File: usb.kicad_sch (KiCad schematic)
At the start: 13 parts

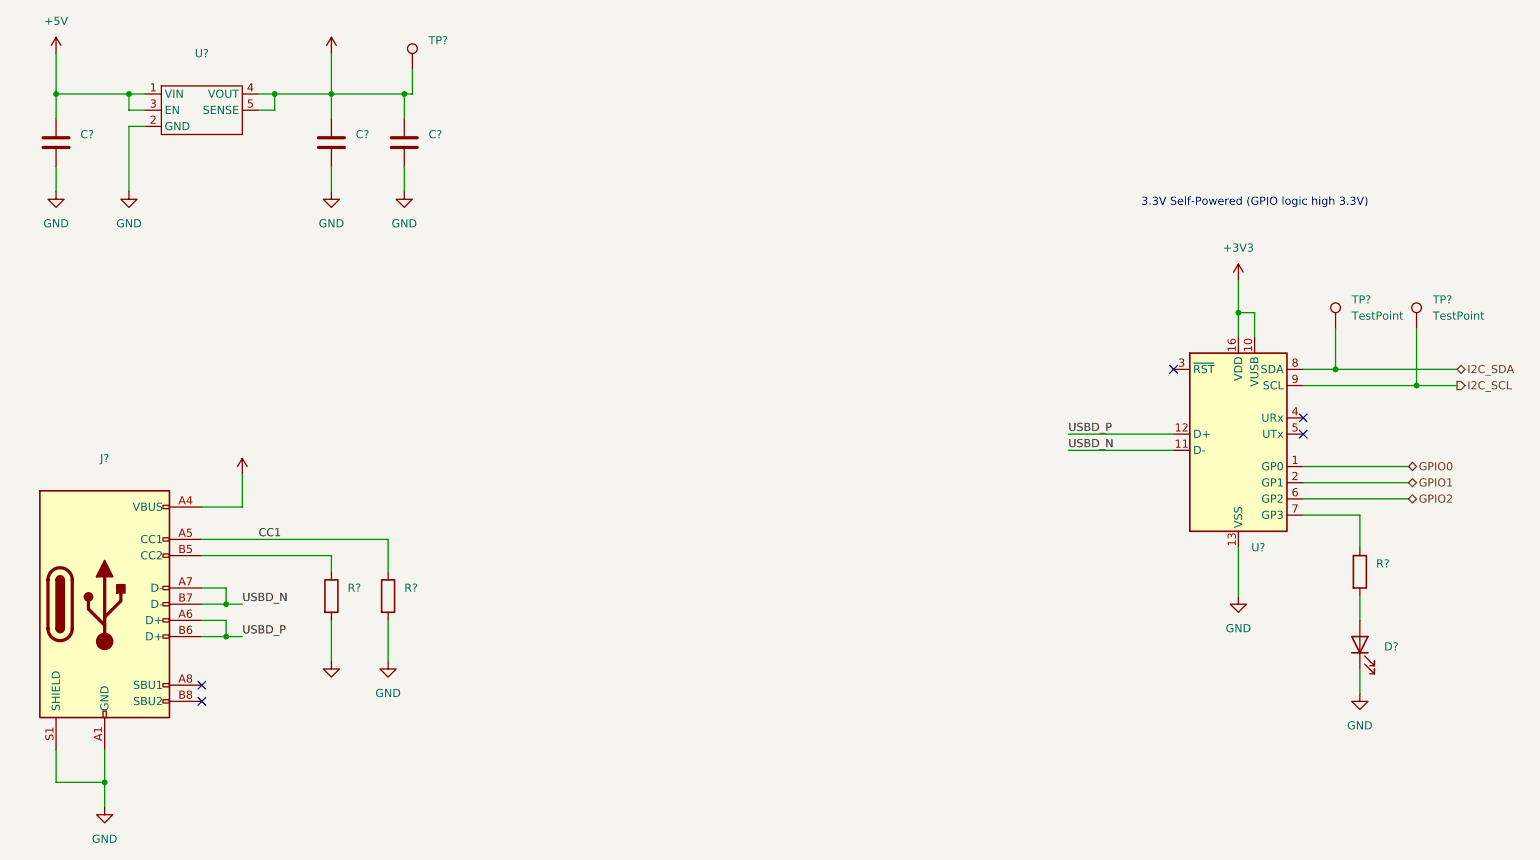
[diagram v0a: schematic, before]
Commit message: WiP: PAC1953 power monitor
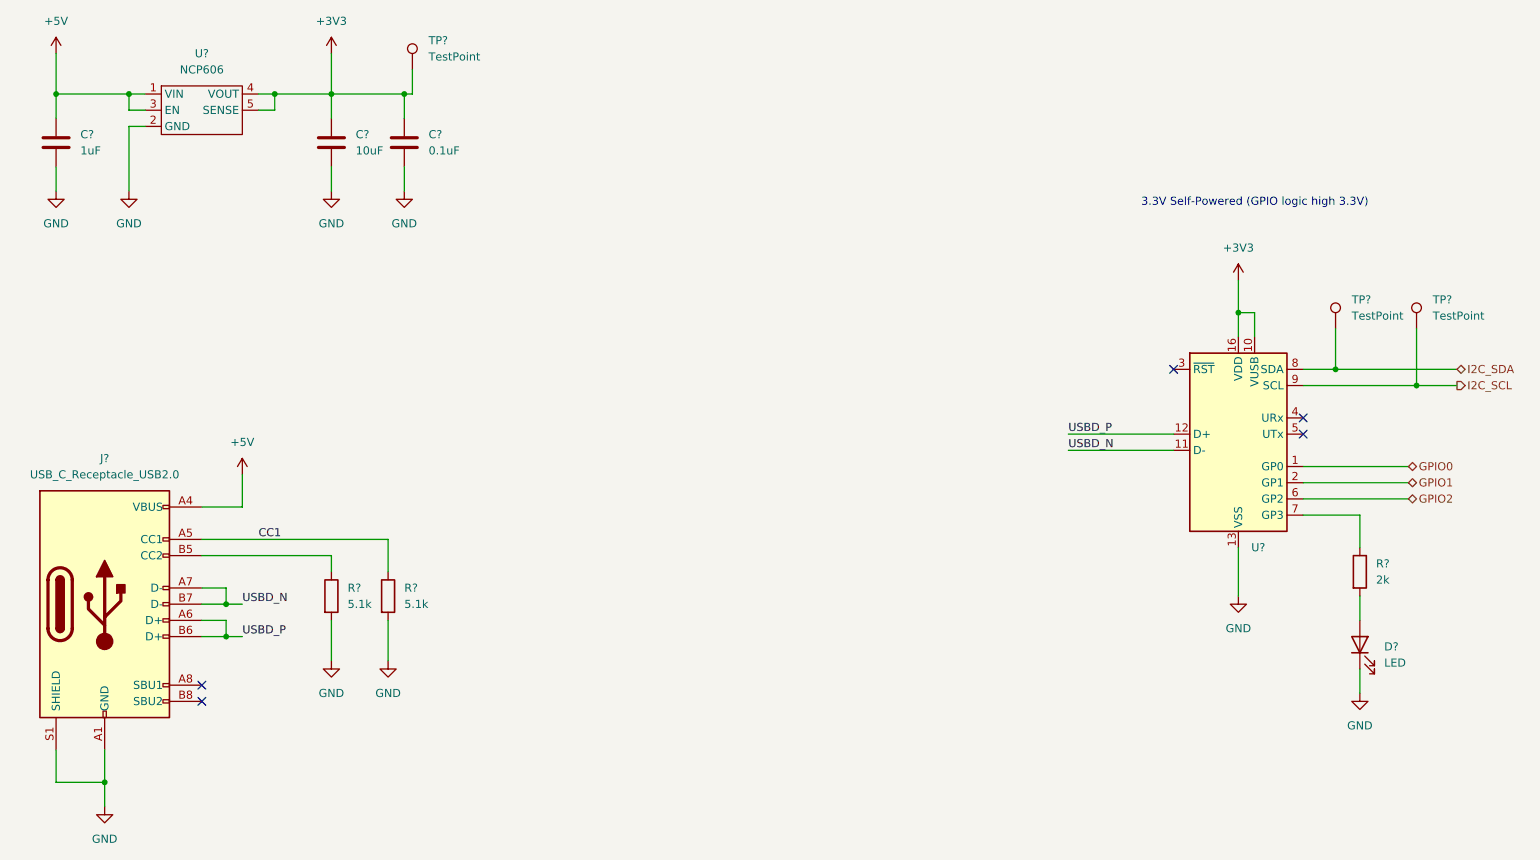
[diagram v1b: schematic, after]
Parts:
- C?: value (none) -> 1uF
- C?: value (none) -> 0.1uF
- C?: value (none) -> 10uF
- D?: value (none) -> LED
- J?: value (none) -> USB_C_Receptacle_USB2.0
- R?: value (none) -> 2k
- R? (x2): value (none) -> 5.1k
- TP?: value (none) -> TestPoint
- U?: value (none) -> NCP606
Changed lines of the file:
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@@
       (effects (font (size 1.27 1.27)) (justify right))
     )
-    (property "Value" "" (id 1) (at 240.03 151.4474 90)
+    (property "Value" "LED" (id 1) (at 240.03 151.4474 90)
       (effects (font (size 1.27 1.27)) (justify right))
     )
@@
       (effects (font (size 1.27 1.27)) hide)
     )
-    (property "Value" "" (id 1) (at 60.96 116.84 0))
+    (property "Value" "+5V" (id 1) (at 60.96 116.84 0))
     (property "Footprint" "" (id 2) (at 60.96 121.92 0)
       (effects (font (size 1.27 1.27)) hide)
@@
     (in_bom yes) (on_board yes) (fields_autoplaced)
     (property "Reference" "J?" (id 0) (at 39.37 119.38 0))
-    (property "Value" "" (id 1) (at 39.37 121.92 0))
+    (property "Value" "USB_C_Receptacle_USB2.0" (id 1) (at 39.37 121.92 0))
     (property "Footprint" "" (id 2) (at 43.18 142.24 0)
       (effects (font (size 1.27 1.27)) hide)
@@
       (effects (font (size 1.27 1.27)) hide)
     )
-    (property "Value" "" (id 1) (at 74.93 50.8 0))
+    (property "Value" "+3V3" (id 1) (at 74.93 50.8 0))
     (property "Footprint" "" (id 2) (at 74.93 55.88 0)
       (effects (font (size 1.27 1.27)) hide)
@@
       (effects (font (size 1.27 1.27)) (justify left))
     )
-    (property "Value" "" (id 1) (at 35.56 71.1199 0)
+    (property "Value" "1uF" (id 1) (at 35.56 71.1199 0)
       (effects (font (size 1.27 1.27)) (justify left))
     )
@@
       (effects (font (size 1.27 1.27)) (justify left))
     )
-    (property "Value" "" (id 1) (at 90.17 71.1199 0)
+    (property "Value" "0.1uF" (id 1) (at 90.17 71.1199 0)
       (effects (font (size 1.27 1.27)) (justify left))
     )
@@
       (effects (font (size 1.27 1.27)) (justify left))
     )
-    (property "Value" "" (id 1) (at 90.17 56.3879 0)
+    (property "Value" "TestPoint" (id 1) (at 90.17 56.3879 0)
       (effects (font (size 1.27 1.27)) (justify left))
     )
@@
       (effects (font (size 1.27 1.27)) (justify left))
     )
-    (property "Value" "" (id 1) (at 238.76 138.4299 0)
+    (property "Value" "2k" (id 1) (at 238.76 138.4299 0)
       (effects (font (size 1.27 1.27)) (justify left))
     )
@@
     (in_bom yes) (on_board yes) (fields_autoplaced)
     (property "Reference" "U?" (id 0) (at 54.61 55.88 0))
-    (property "Value" "" (id 1) (at 54.61 58.42 0))
+    (property "Value" "NCP606" (id 1) (at 54.61 58.42 0))
     (property "Footprint" "" (id 2) (at 52.07 64.77 0)
       (effects (font (size 1.27 1.27)) hide)
@@
       (effects (font (size 1.27 1.27)) (justify left))
     )
-    (property "Value" "" (id 1) (at 86.36 142.2399 0)
+    (property "Value" "5.1k" (id 1) (at 86.36 142.2399 0)
       (effects (font (size 1.27 1.27)) (justify left))
     )
@@
       (effects (font (size 1.27 1.27)) (justify left))
     )
-    (property "Value" "" (id 1) (at 78.74 71.1199 0)
+    (property "Value" "10uF" (id 1) (at 78.74 71.1199 0)
       (effects (font (size 1.27 1.27)) (justify left))
     )
@@
       (effects (font (size 1.27 1.27)) (justify left))
     )
-    (property "Value" "" (id 1) (at 77.47 142.2399 0)
+    (property "Value" "5.1k" (id 1) (at 77.47 142.2399 0)
       (effects (font (size 1.27 1.27)) (justify left))
     )
@@
       (effects (font (size 1.27 1.27)) hide)
     )
-    (property "Value" "" (id 1) (at 74.93 156.21 0))
+    (property "Value" "GND" (id 1) (at 74.93 156.21 0))
     (property "Footprint" "" (id 2) (at 74.93 151.13 0)
       (effects (font (size 1.27 1.27)) hide)

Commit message: PAC1953 shunt resistors, terminals
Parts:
- added U?: (no value), symbol ik:TPD2E001DRSR
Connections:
- net +5V: now also U?.1 (Vcc)
- net GND: now also U?.4 (GND)
- net USBD_N: now also U?.3 (IO1)
- net USBD_P: now also U?.6 (IO2)
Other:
- moved on the sheet: R?

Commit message: ERC
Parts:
- gave numbers to parts that had none: 14
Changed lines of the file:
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@@
   (junction (at 85.09 147.32) (diameter 0) (color 0 0 0 0)
+  )
+  (junction (at 60.96 127) (diameter 0) (color 0 0 0 0)
   )
   (junction (at 82.55 142.24) (diameter 0) (color 0 0 0 0)
@@
     (stroke (width 0) (type default) (color 0 0 0 0))
   )
+  (wire (pts (xy 60.96 127) (xy 67.31 127))
+    (stroke (width 0) (type default) (color 0 0 0 0))
+  )
+  (wire (pts (xy 67.31 125.73) (xy 67.31 127))
+    (stroke (width 0) (type default) (color 0 0 0 0))
+  )
   (wire (pts (xy 54.61 142.24) (xy 58.42 142.24))
     (stroke (width 0) (type default) (color 0 0 0 0))
@@
     (stroke (width 0) (type default) (color 0 0 0 0))
   )
+  (wire (pts (xy 45.72 167.64) (xy 45.72 170.18))
+    (stroke (width 0) (type default) (color 0 0 0 0))
+  )
   (wire (pts (xy 54.61 134.62) (xy 105.41 134.62))
     (stroke (width 0) (type default) (color 0 0 0 0))
@@
   )
   (wire (pts (xy 63.5 64.77) (xy 66.04 64.77))
+    (stroke (width 0) (type default) (color 0 0 0 0))
+  )
+  (wire (pts (xy 45.72 170.18) (xy 39.37 170.18))
     (stroke (width 0) (type default) (color 0 0 0 0))
   )
@@
   (symbol (lib_id "Device:LED") (at 236.22 148.59 90) (unit 1)
     (in_bom yes) (on_board yes) (fields_autoplaced)
-    (property "Reference" "D?" (id 0) (at 240.03 148.9074 90)
+    (property "Reference" "D1" (id 0) (at 240.03 148.9074 90)
       (effects (font (size 1.27 1.27)) (justify right))
     )
@@
   (symbol (lib_id "Connector:USB_C_Receptacle_USB2.0") (at 39.37 142.24 0) (unit 1)
     (in_bom yes) (on_board yes) (fields_autoplaced)
-    (property "Reference" "J?" (id 0) (at 39.37 119.38 0))
+    (property "Reference" "J7" (id 0) (at 39.37 119.38 0))
     (property "Value" "USB_C_Receptacle_USB2.0" (id 1) (at 39.37 121.92 0))
     (property "Footprint" "" (id 2) (at 43.18 142.24 0)
@@
     (pin "1")
   )
+  (symbol (lib_id "power:PWR_FLAG") (at 67.31 125.73 0) (unit 1)
+    (in_bom yes) (on_board yes) (fields_autoplaced)
+    (property "Reference" "#FLG02" (id 0) (at 67.31 123.825 0)
+      (effects (font (size 1.27 1.27)) hide)
+    )
+    (property "Value" "" (id 1) (at 67.31 120.65 0))
+    (property "Footprint" "" (id 2) (at 67.31 125.73 0)
+      (effects (font (size 1.27 1.27)) hide)
+    )
+    (property "Datasheet" "~" (id 3) (at 67.31 125.73 0)
+      (effects (font (size 1.27 1.27)) hide)
+    )
+    (pin "1")
+  )
   (symbol (lib_id "power:GND") (at 114.3 151.13 0) (unit 1)
     (in_bom yes) (on_board yes) (fields_autoplaced)
@@
     (pin "1")
   )
+  (symbol (lib_id "power:PWR_FLAG") (at 45.72 167.64 0) (unit 1)
+    (in_bom yes) (on_board yes) (fields_autoplaced)
+    (property "Reference" "#FLG01" (id 0) (at 45.72 165.735 0)
+      (effects (font (size 1.27 1.27)) hide)
+    )
+    (property "Value" "PWR_FLAG" (id 1) (at 45.72 162.56 0))
+    (property "Footprint" "" (id 2) (at 45.72 167.64 0)
+      (effects (font (size 1.27 1.27)) hide)
+    )
+    (property "Datasheet" "~" (id 3) (at 45.72 167.64 0)
+      (effects (font (size 1.27 1.27)) hide)
+    )
+    (pin "1")
+  )
   (symbol (lib_id "ik:TPD2E001DRSR") (at 82.55 161.29 0) (unit 1)
     (in_bom yes) (on_board yes) (fields_autoplaced)
-    (property "Reference" "U?" (id 0) (at 90.17 160.6549 0)
+    (property "Reference" "U3" (id 0) (at 90.17 160.6549 0)
       (effects (font (size 1.27 1.27)) (justify left))
     )
@@
   (symbol (lib_id "Device:C") (at 31.75 69.85 0) (unit 1)
     (in_bom yes) (on_board yes) (fields_autoplaced)
-    (property "Reference" "C?" (id 0) (at 35.56 68.5799 0)
+    (property "Reference" "C3" (id 0) (at 35.56 68.5799 0)
       (effects (font (size 1.27 1.27)) (justify left))
     )
@@
   (symbol (lib_id "Device:C") (at 86.36 69.85 0) (unit 1)
     (in_bom yes) (on_board yes) (fields_autoplaced)
-    (property "Reference" "C?" (id 0) (at 90.17 68.5799 0)
+    (property "Reference" "C5" (id 0) (at 90.17 68.5799 0)
       (effects (font (size 1.27 1.27)) (justify left))
     )
@@
   (symbol (lib_id "Connector:TestPoint") (at 87.63 58.42 0) (unit 1)
     (in_bom yes) (on_board yes) (fields_autoplaced)
-    (property "Reference" "TP?" (id 0) (at 90.17 53.8479 0)
+    (property "Reference" "TP13" (id 0) (at 90.17 53.8479 0)
       (effects (font (size 1.27 1.27)) (justify left))
     )
@@
   (symbol (lib_id "Device:R") (at 236.22 137.16 0) (unit 1)
     (in_bom yes) (on_board yes) (fields_autoplaced)
-    (property "Reference" "R?" (id 0) (at 238.76 135.8899 0)
+    (property "Reference" "R9" (id 0) (at 238.76 135.8899 0)
       (effects (font (size 1.27 1.27)) (justify left))
     )
@@
   (symbol (lib_id "ik:NCP606") (at 52.07 64.77 0) (unit 1)
     (in_bom yes) (on_board yes) (fields_autoplaced)
-    (property "Reference" "U?" (id 0) (at 54.61 55.88 0))
+    (property "Reference" "U2" (id 0) (at 54.61 55.88 0))
     (property "Value" "NCP606" (id 1) (at 54.61 58.42 0))
     (property "Footprint" "" (id 2) (at 52.07 64.77 0)
@@
   (symbol (lib_id "Device:R") (at 114.3 140.97 0) (unit 1)
     (in_bom yes) (on_board yes) (fields_autoplaced)
-    (property "Reference" "R?" (id 0) (at 116.84 139.6999 0)
+    (property "Reference" "R8" (id 0) (at 116.84 139.6999 0)
       (effects (font (size 1.27 1.27)) (justify left))
     )
@@
   (symbol (lib_id "Connector:TestPoint") (at 245.11 99.06 0) (unit 1)
     (in_bom yes) (on_board yes) (fields_autoplaced)
-    (property "Reference" "TP?" (id 0) (at 247.65 94.4879 0)
+    (property "Reference" "TP15" (id 0) (at 247.65 94.4879 0)
       (effects (font (size 1.27 1.27)) (justify left))
     )
@@
   (symbol (lib_id "Interface_USB:MCP2221AxML") (at 217.17 118.11 0) (unit 1)
     (in_bom yes) (on_board yes) (fields_autoplaced)
-    (property "Reference" "U?" (id 0) (at 219.1894 133.35 0)
+    (property "Reference" "U4" (id 0) (at 219.1894 133.35 0)
       (effects (font (size 1.27 1.27)) (justify left))
     )
@@
   (symbol (lib_id "Device:C") (at 74.93 69.85 0) (unit 1)
     (in_bom yes) (on_board yes) (fields_autoplaced)
-    (property "Reference" "C?" (id 0) (at 78.74 68.5799 0)
+    (property "Reference" "C4" (id 0) (at 78.74 68.5799 0)
       (effects (font (size 1.27 1.27)) (justify left))
     )
@@
   (symbol (lib_id "Device:R") (at 105.41 140.97 0) (unit 1)
     (in_bom yes) (on_board yes) (fields_autoplaced)
-    (property "Reference" "R?" (id 0) (at 107.95 139.6999 0)
+    (property "Reference" "R7" (id 0) (at 107.95 139.6999 0)
       (effects (font (size 1.27 1.27)) (justify left))
     )
@@
   (symbol (lib_id "Connector:TestPoint") (at 232.41 99.06 0) (unit 1)
     (in_bom yes) (on_board yes) (fields_autoplaced)
-    (property "Reference" "TP?" (id 0) (at 234.95 94.4879 0)
-      (effects (font (size 1.27 1.27)) (justify left))
-    )
+    (property "Reference" "TP14" (id 0) (at 234.95 94.4879 0)
+      (effects (font (size 1.27 1.27)) (justify left))
+    )
